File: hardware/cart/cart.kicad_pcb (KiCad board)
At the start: 2 copper layers, 40.1 x 35.8 mm, 6 parts, among them J1 Front Edge, J2 Back Edge, U1 Pro Micro

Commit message: Update cart breakaway tab to use drills (1.0-dev2)
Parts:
- added REF**: BREAKAWAY_HOLE, cart:BREAKAWAY_HOLE, F.Cu at (129.7, 126.7)
- added REF**: BREAKAWAY_HOLE, cart:BREAKAWAY_HOLE, F.Cu at (132.0, 126.7)
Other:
- outline, holes or cut-outs redrawn
- board text added: "1.0-dev2"
- board text removed: "1.0-dev1"
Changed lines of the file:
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@@
   (general
     (thickness 1.6)
-    (drawings 56)
+    (drawings 52)
     (tracks 54)
     (zones 0)
-    (modules 6)
+    (modules 8)
     (nets 23)
   )
@@
   (title_block
     (title "Arduboy CE Cart")
-    (date 2021-03-04)
-    (rev 1.0-dev0)
+    (date 2021-03-08)
+    (rev 1.0-dev2)
   )
   (layers
     (0 F.Cu signal)
     (31 B.Cu signal)
-    (32 B.Adhes user hide)
-    (33 F.Adhes user hide)
-    (34 B.Paste user hide)
+    (32 B.Adhes user)
+    (33 F.Adhes user)
+    (34 B.Paste user)
     (35 F.Paste user)
     (36 B.SilkS user hide)
     (37 F.SilkS user)
     (38 B.Mask user hide)
-    (39 F.Mask user)
-    (40 Dwgs.User user hide)
-    (41 Cmts.User user hide)
-    (42 Eco1.User user hide)
-    (43 Eco2.User user hide)
+    (39 F.Mask user hide)
+    (40 Dwgs.User user)
+    (41 Cmts.User user)
+    (42 Eco1.User user)
+    (43 Eco2.User user)
     (44 Edge.Cuts user)
-    (45 Margin user hide)
-    (46 B.CrtYd user hide)
+    (45 Margin user)
+    (46 B.CrtYd user)
     (47 F.CrtYd user)
-    (48 B.Fab user hide)
+    (48 B.Fab user)
     (49 F.Fab user)
   )
@@
     (mod_text_size 1 1)
     (mod_text_width 0.15)
-    (pad_size 0.508 0.508)
+    (pad_size 0.508 4.25)
     (pad_drill 0.508)
     (pad_to_mask_clearance 0.0508)
@@
       (drillshape 0)
       (scaleselection 1)
-      (outputdirectory "gerber/cart-1.0dev1"))
+      (outputdirectory "gerber/cart-1.0dev2"))
   )
   (net 0 "")
@@
   )
   (module cart:BREAKAWAY_HOLE (layer F.Cu)
+    (at 129.667 126.712)
+    (fp_text reference REF** (at 0 2.54) (layer F.SilkS) hide
+      (effects (font (size 1 1) (thickness 0.15)))
+    )
+    (fp_text value BREAKAWAY_HOLE (at 0 -2.54) (layer F.Fab) hide
+      (effects (font (size 1 1) (thickness 0.15)))
+    )
+    (pad "" np_thru_hole oval (at 0 0.127) (size 0.508 4.25) (drill oval 0.508 4.25) (layers *.Cu *.Mask))
+  )
+  (module cart:BREAKAWAY_HOLE (layer F.Cu)
+    (at 131.953 126.712)
+    (fp_text reference REF** (at 0 2.54) (layer F.SilkS) hide
+      (effects (font (size 1 1) (thickness 0.15)))
+    )
+    (fp_text value BREAKAWAY_HOLE (at 0 -2.54) (layer F.Fab) hide
+      (effects (font (size 1 1) (thickness 0.15)))
+    )
+    (pad "" np_thru_hole oval (at 0 0.127) (size 0.508 4.25) (drill oval 0.508 4.25) (layers *.Cu *.Mask))
+  )
+  (module cart:BREAKAWAY_HOLE (layer F.Cu)
     (at 131.699 124.841)
     (fp_text reference REF** (at 0 2.54) (layer F.SilkS) hide
@@
       (effects (font (size 1 1) (thickness 0.15)))
     )
+    (fp_line (start -13.97 3.81) (end -13.97 -3.81) (layer F.SilkS) (width 0.15))
+    (fp_line (start 16.51 -8.89) (end 16.51 8.89) (layer F.SilkS) (width 0.15))
+    (fp_line (start -16.51 -8.89) (end 16.51 -8.89) (layer F.SilkS) (width 0.15))
+    (fp_line (start -16.51 -3.81) (end -16.51 -8.89) (layer F.SilkS) (width 0.15))
+    (fp_line (start -16.51 -3.81) (end -13.97 -3.81) (layer F.SilkS) (width 0.15))
+    (fp_line (start -16.51 3.81) (end -16.51 -3.81) (layer F.SilkS) (width 0.15))
+    (fp_line (start -13.97 3.81) (end -16.51 3.81) (layer F.SilkS) (width 0.15))
+    (fp_line (start -16.51 8.89) (end -16.51 3.81) (layer F.SilkS) (width 0.15))
     (fp_line (start -16.51 8.89) (end 16.51 8.89) (layer F.SilkS) (width 0.15))
-    (fp_line (start -16.51 8.89) (end -16.51 3.81) (layer F.SilkS) (width 0.15))
-    (fp_line (start -13.97 3.81) (end -16.51 3.81) (layer F.SilkS) (width 0.15))
-    (fp_line (start -16.51 3.81) (end -16.51 -3.81) (layer F.SilkS) (width 0.15))
-    (fp_line (start -16.51 -3.81) (end -13.97 -3.81) (layer F.SilkS) (width 0.15))
-    (fp_line (start -16.51 -3.81) (end -16.51 -8.89) (layer F.SilkS) (width 0.15))
-    (fp_line (start -16.51 -8.89) (end 16.51 -8.89) (layer F.SilkS) (width 0.15))
-    (fp_line (start 16.51 -8.89) (end 16.51 8.89) (layer F.SilkS) (width 0.15))
-    (fp_line (start -13.97 3.81) (end -13.97 -3.81) (layer F.SilkS) (width 0.15))
     (pad 24 thru_hole circle (at -12.7 -7.62) (size 1.6 1.6) (drill 1.1) (layers *.Cu *.Mask F.SilkS)
       (net 12 "Net-(J2-Pad12)"))
@@
       (net 3 "Net-(J1-Pad1)"))
   )
+  (gr_line (start 129.433 128.397) (end 129.794 128.397) (layer Edge.Cuts) (width 0.2))
+  (gr_line (start 129.794 128.397) (end 129.794 128.651) (layer Edge.Cuts) (width 0.2))
   (gr_line (start 159.75 94.611) (end 159.75 120.142) (layer Edge.Cuts) (width 0.2))
   (gr_arc (start 157.972 94.611) (end 159.75 94.611) (angle -90) (layer Edge.Cuts) (width 0.2))
@@
   (gr_arc (start 153.67 98.85) (end 153.67 101.39) (angle -180) (layer Edge.Cuts) (width 0.2))
   (gr_arc (start 125.73 98.85) (end 125.73 96.31) (angle -180) (layer Edge.Cuts) (width 0.2))
-  (gr_text JLCJLCJLCJLC (at 123.444 103.378 90) (layer B.SilkS)
-    (effects (font (size 0.762 0.762) (thickness 0.127)) (justify left mirror))
+  (gr_text JLCJLCJLCJLC (at 121.412 108.204 90) (layer B.SilkS)
+    (effects (font (size 0.762 0.762) (thickness 0.127)) (justify mirror))
   )
   (gr_poly (pts (xy 154.4955 100.3105) (xy 160.147 100.3105) (xy 160.147 100.8185) (xy 154.4955 100.8185)) (layer F.Mask) (width 0.2))
@@
   (gr_poly (pts (xy 154.4955 98.0245) (xy 160.147 98.0245) (xy 160.147 98.5325) (xy 154.4955 98.5325)) (layer F.Mask) (width 0.2))
   (gr_poly (pts (xy 154.4955 96.8815) (xy 160.147 96.8815) (xy 160.147 97.3895) (xy 154.4955 97.3895)) (layer F.Mask) (width 0.2))
-  (gr_line (start 131.826 124.714) (end 132.207 124.714) (layer Edge.Cuts) (width 0.2))
+  (gr_line (start 131.826 128.397) (end 132.187 128.397) (layer Edge.Cuts) (width 0.2))
   (gr_line (start 129.794 128.651) (end 131.826 128.651) (layer Edge.Cuts) (width 0.2))
-  (gr_line (start 131.826 124.714) (end 131.826 128.651) (layer Edge.Cuts) (width 0.2))
-  (gr_line (start 129.794 124.714) (end 129.794 128.651) (layer Edge.Cuts) (width 0.2))
+  (gr_line (start 131.826 128.397) (end 131.826 128.651) (layer Edge.Cuts) (width 0.2))
   (gr_text github.com/menehune23/arduboy-ce (at 139.7 122.301) (layer B.SilkS)
     (effects (font (size 0.762 0.762) (thickness 0.127)) (justify mirror))
@@
     (effects (font (size 1.27 1.27) (thickness 0.254)) (justify mirror))
   )
-  (gr_line (start 132.461 128.651) (end 132.207 128.397) (layer Edge.Cuts) (width 0.2))
-  (gr_line (start 129.413 128.397) (end 129.159 128.651) (layer Edge.Cuts) (width 0.2))
-  (gr_line (start 129.413 124.714) (end 129.794 124.714) (layer Edge.Cuts) (width 0.2))
-  (gr_line (start 132.207 124.714) (end 132.207 128.397) (layer Edge.Cuts) (width 0.2))
-  (gr_line (start 129.413 124.714) (end 129.413 128.397) (layer Edge.Cuts) (width 0.2))
-  (gr_line (start 157.988 128.651) (end 132.461 128.651) (layer Edge.Cuts) (width 0.2))
+  (gr_line (start 132.441 128.651) (end 132.187 128.397) (layer Edge.Cuts) (width 0.2))
+  (gr_line (start 129.433 128.397) (end 129.179 128.651) (layer Edge.Cuts) (width 0.2))
+  (gr_line (start 157.988 128.651) (end 132.441 128.651) (layer Edge.Cuts) (width 0.2))
   (gr_poly (pts (xy 154.4955 100.3105) (xy 160.147 100.3105) (xy 160.147 100.8185) (xy 154.4955 100.8185)) (layer F.Cu) (width 0.2))
   (gr_poly (pts (xy 154.4955 99.1675) (xy 160.147 99.1675) (xy 160.147 99.6755) (xy 154.4955 99.6755)) (layer F.Cu) (width 0.2))
@@
   (gr_line (start 120.65 120.901) (end 120.65 127.127) (layer Edge.Cuts) (width 0.2))
   (gr_line (start 158.75 120.904) (end 158.75 127.127) (layer Edge.Cuts) (width 0.2))
-  (gr_circle (center 174.625 93.98) (end 177.421885 93.98) (layer Cmts.User) (width 0.15))
-  (gr_circle (center 174.625 88.265) (end 177.421885 88.265) (layer Cmts.User) (width 0.15))
   (gr_poly (pts (xy 154.4955 98.0245) (xy 160.147 98.0245) (xy 160.147 98.5325) (xy 154.4955 98.5325)) (layer F.Cu) (width 0.2))
   (gr_poly (pts (xy 160.4645 124.6505) (xy 160.401 129.667) (xy 118.618 129.667) (xy 118.6815 124.6505)) (layer B.Mask) (width 0.1))
   (gr_poly (pts (xy 160.401 124.6505) (xy 160.401 129.667) (xy 118.618 129.667) (xy 118.618 124.6505)) (layer F.Mask) (width 0.1))
   (gr_line (start 121.428 92.833) (end 157.972 92.833) (layer Edge.Cuts) (width 0.2))
-  (gr_text 1.0-dev1 (at 121.412 103.124 90) (layer B.Cu)
-    (effects (font (size 1.016 1.016) (thickness 0.2286)) (justify left mirror))
+  (gr_text 1.0-dev2 (at 139.7 94.488) (layer B.Cu)
+    (effects (font (size 1.016 1.016) (thickness 0.2286)) (justify mirror))
   )
   (gr_line (start 121.412 128.651) (end 120.65 127.127) (layer Edge.Cuts) (width 0.2))
   (gr_line (start 157.988 128.651) (end 158.75 127.127) (layer Edge.Cuts) (width 0.2))
   (gr_poly (pts (xy 139.7 123.698) (xy 137.922 122.174) (xy 141.478 122.174)) (layer F.SilkS) (width 0.2))
-  (gr_line (start 121.412 128.651) (end 129.159 128.651) (layer Edge.Cuts) (width 0.2))
+  (gr_line (start 121.412 128.651) (end 129.179 128.651) (layer Edge.Cuts) (width 0.2))
   (segment (start 128.27 126.619) (end 128.27 123.19) (width 0.508) (layer F.Cu) (net 1))
   (via (at 134.62 111.76) (size 0.6) (drill 0.3) (layers F.Cu B.Cu) (net 1))

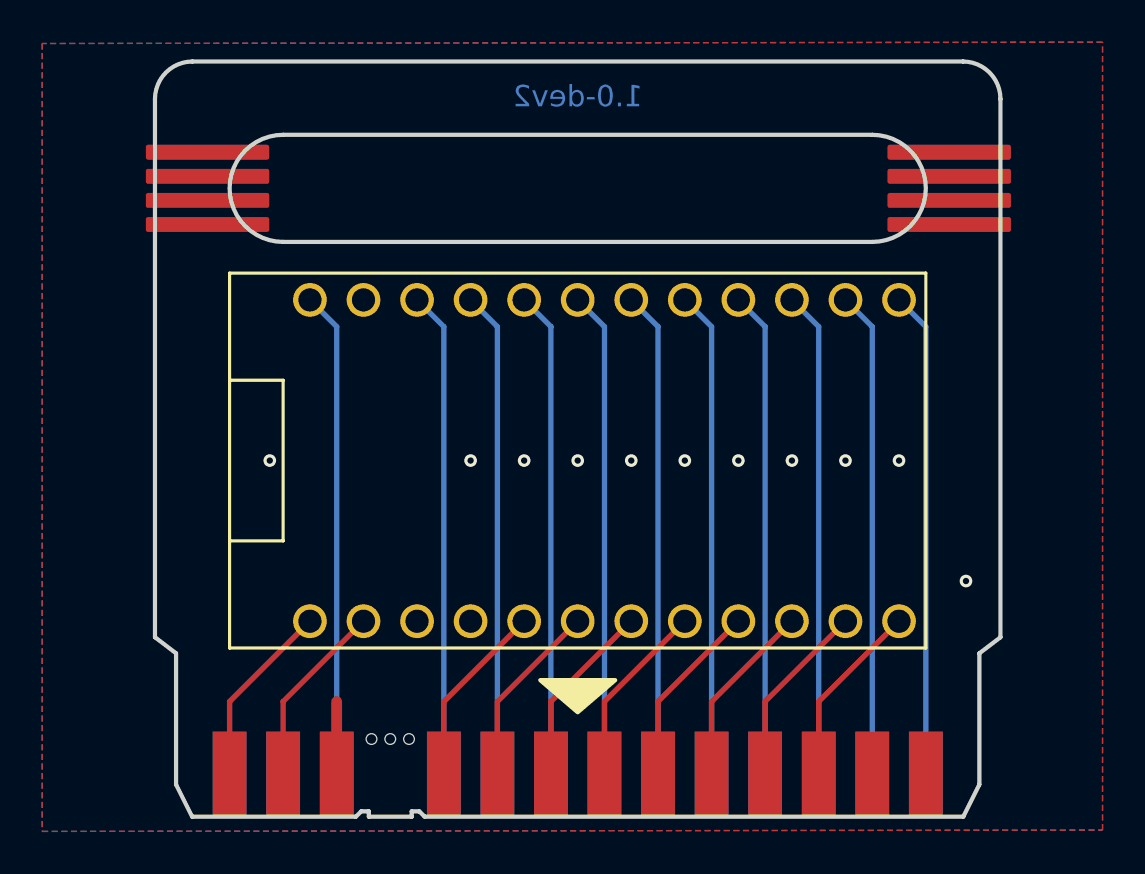
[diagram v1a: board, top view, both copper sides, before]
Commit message: Update system and cart
- Shorten cart by 1mm to account for other connector brand
- Use 1-pin header for charger board support
- Fix diode footprint
- Bump cart/system versions (no gerbers yet)
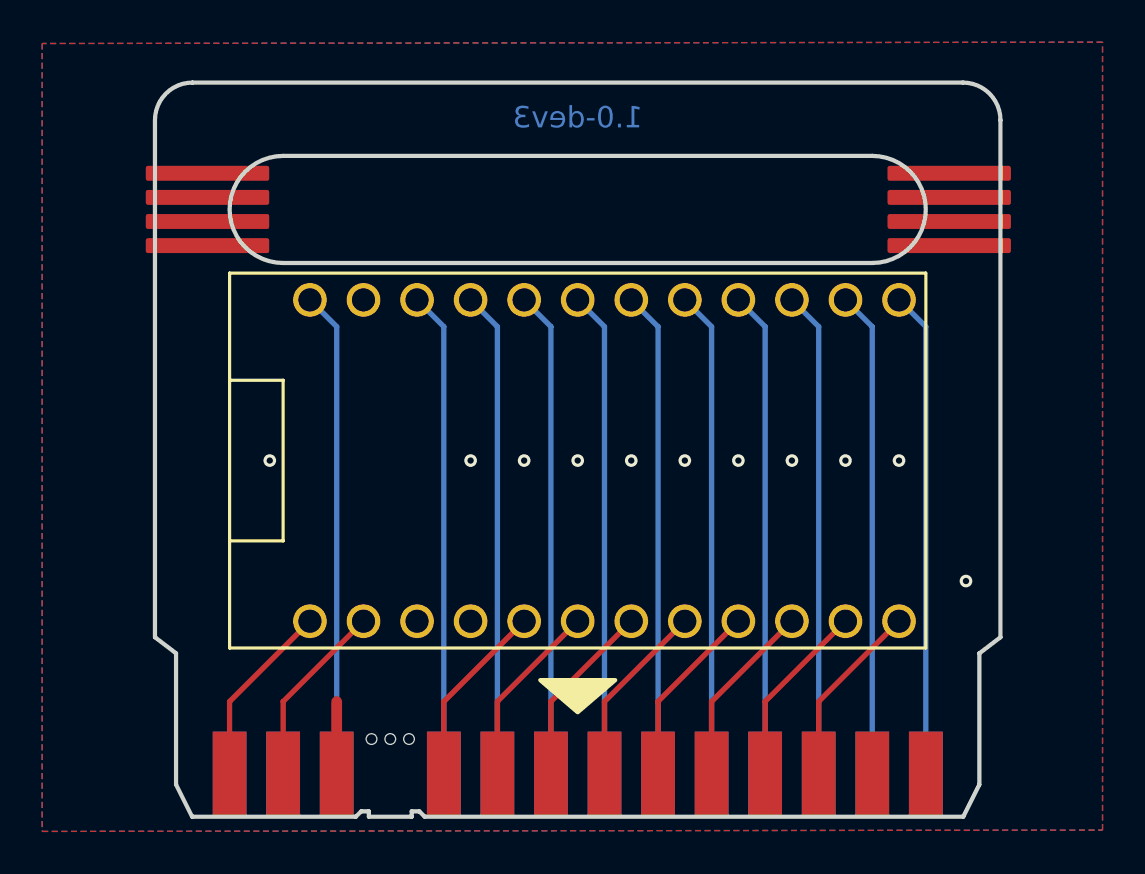
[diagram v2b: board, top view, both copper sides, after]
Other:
- board size 40.1 x 35.8 mm -> 40.1 x 34.8 mm
- board text added: "1.0-dev3"
- board text removed: "1.0-dev2"
